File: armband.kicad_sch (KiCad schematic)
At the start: 10 parts, among them IC1 QSMP-1570, SW1 SW_MEC_5G, SW2 SW_MEC_5G

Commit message: progressed charging and gas gauge schematic
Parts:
- added C3, C7: C_Small, symbol Device:C_Small
- renumbered C4 to C1, C3 to C2, R5 to R1, R1 to R2, R2 to R3, R3 to R5, SW2 to SW1, SW1 to SW2
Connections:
- net GND: now also C3.2, C7.2
- net QSMP_VBUS: now also C3.1, C7.1
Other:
- moved on the sheet: C1, R1, R2, R3, SW1

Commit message: added buck
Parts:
- added C5, C8: C_Small, symbol Device:C_Small
- R2, R3: MFN (none) -> 667-ERJ-1GNJ103C
- renumbered C7 to C4
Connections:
- net QSMP_VIN is gone; now on net +3V3: IC1.49 (VIN_1), IC1.50 (VIN_2)
- net +3V3: now also C5.1, C8.1
- net GND: now also C5.2, C8.2
- net QSMP_SCL: now also R2.2; no longer R3.2
- net QSMP_SDA: now also R3.2; no longer R2.2

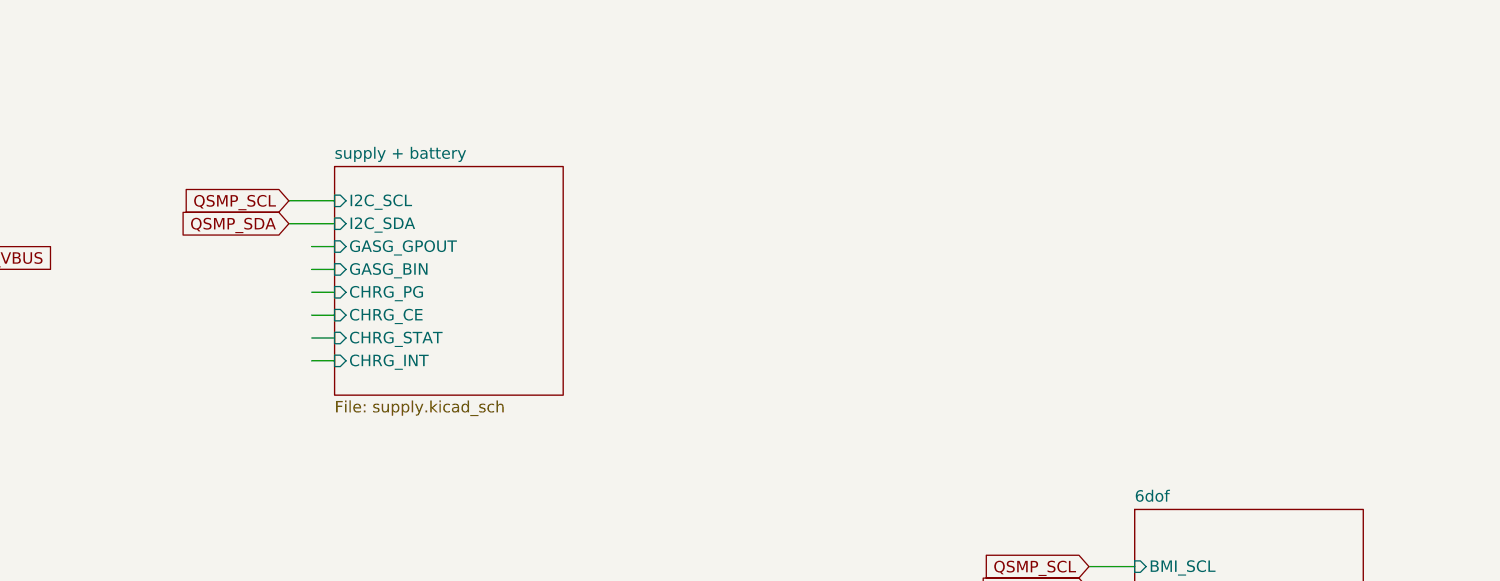
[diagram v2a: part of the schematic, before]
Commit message: added usb connector
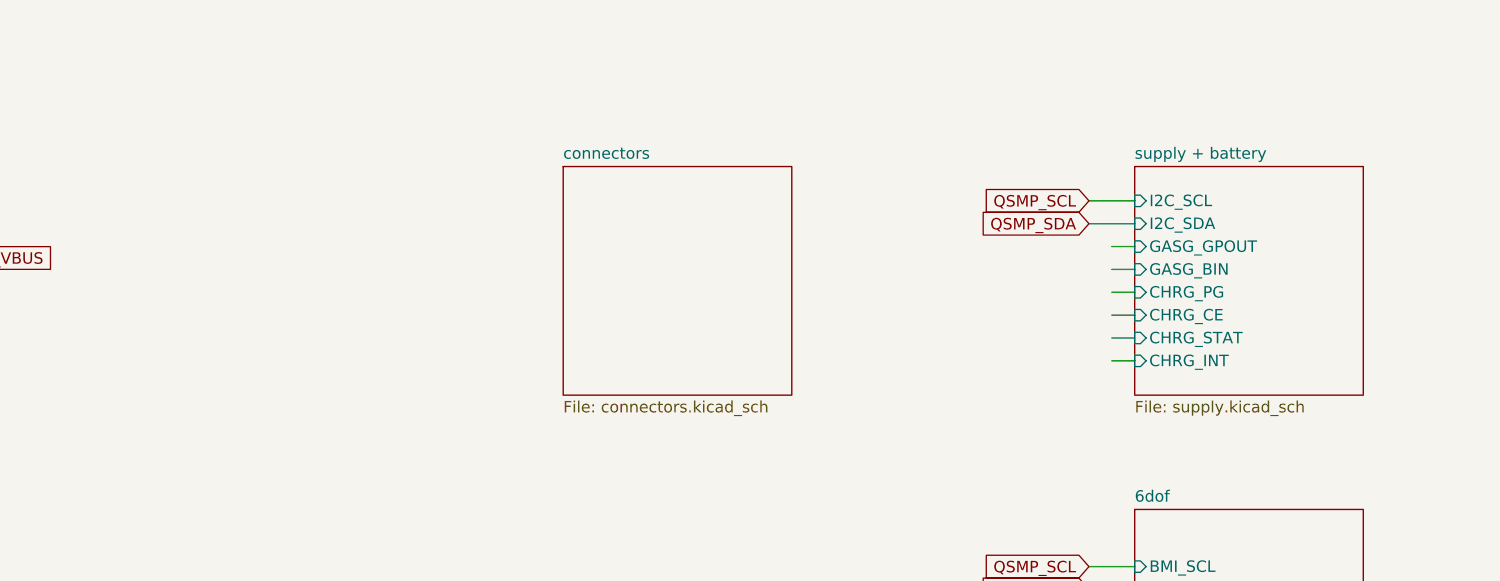
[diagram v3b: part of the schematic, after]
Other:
- added sheet connectors (connectors.kicad_sch)
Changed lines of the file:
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@@
     (stroke (width 0) (type default))
   )
-  (wire (pts (xy 276.86 41.91) (xy 279.4 41.91))
+  (wire (pts (xy 365.76 41.91) (xy 368.3 41.91))
     (stroke (width 0) (type default))
   )
@@
     (stroke (width 0) (type default))
   )
-  (wire (pts (xy 274.32 31.75) (xy 279.4 31.75))
+  (wire (pts (xy 363.22 31.75) (xy 368.3 31.75))
     (stroke (width 0) (type default))
   )
@@
     (stroke (width 0) (type default))
   )
-  (wire (pts (xy 274.32 29.21) (xy 279.4 29.21))
+  (wire (pts (xy 363.22 29.21) (xy 368.3 29.21))
     (stroke (width 0) (type default))
   )
@@
     (stroke (width 0) (type default))
   )
-  (wire (pts (xy 276.86 34.29) (xy 279.4 34.29))
+  (wire (pts (xy 365.76 34.29) (xy 368.3 34.29))
     (stroke (width 0) (type default))
   )
@@
     (stroke (width 0) (type default))
   )
-  (wire (pts (xy 276.86 39.37) (xy 279.4 39.37))
+  (wire (pts (xy 365.76 39.37) (xy 368.3 39.37))
     (stroke (width 0) (type default))
   )
@@
     (stroke (width 0) (type default))
   )
-  (wire (pts (xy 276.86 36.83) (xy 279.4 36.83))
+  (wire (pts (xy 365.76 36.83) (xy 368.3 36.83))
     (stroke (width 0) (type default))
   )
@@
     (stroke (width 0) (type default))
   )
-  (wire (pts (xy 276.86 46.99) (xy 279.4 46.99))
+  (wire (pts (xy 365.76 46.99) (xy 368.3 46.99))
     (stroke (width 0) (type default))
   )
@@
     (stroke (width 0) (type default))
   )
-  (wire (pts (xy 276.86 44.45) (xy 279.4 44.45))
+  (wire (pts (xy 365.76 44.45) (xy 368.3 44.45))
     (stroke (width 0) (type default))
   )
@@
     )
   )
-  (global_label "QSMP_SDA" (shape input) (at 274.32 31.75 180) (fields_autoplaced)
-    (effects (font (size 1.27 1.27)) (justify right))
-    (property "Intersheetrefs" "${INTERSHEET_REFS}" (at 261.6171 31.75 0)
-      (effects (font (size 1.27 1.27)) (justify right) hide)
-    )
-  )
-  (global_label "QSMP_SCL" (shape input) (at 274.32 29.21 180) (fields_autoplaced)
-    (effects (font (size 1.27 1.27)) (justify right))
-    (property "Intersheetrefs" "${INTERSHEET_REFS}" (at 261.6776 29.21 0)
+  (global_label "QSMP_SDA" (shape input) (at 363.22 31.75 180) (fields_autoplaced)
+    (effects (font (size 1.27 1.27)) (justify right))
+    (property "Intersheetrefs" "${INTERSHEET_REFS}" (at 350.5171 31.75 0)
+      (effects (font (size 1.27 1.27)) (justify right) hide)
+    )
+  )
+  (global_label "QSMP_SCL" (shape input) (at 363.22 29.21 180) (fields_autoplaced)
+    (effects (font (size 1.27 1.27)) (justify right))
+    (property "Intersheetrefs" "${INTERSHEET_REFS}" (at 350.5776 29.21 0)
       (effects (font (size 1.27 1.27)) (justify right) hide)
     )
@@
     )
   )
+  (sheet (at 304.8 25.4) (size 25.4 25.4) (fields_autoplaced)
+    (stroke (width 0.1524) (type solid))
+    (fill (color 0 0 0 0.0000))
+    (property "Sheetname" "connectors" (at 304.8 24.6884 0)
+      (effects (font (size 1.27 1.27)) (justify left bottom))
+    )
+    (property "Sheetfile" "connectors.kicad_sch" (at 304.8 51.3846 0)
+      (effects (font (size 1.27 1.27)) (justify left top))
+    )
+    (instances
+      (project "armband"
+        (path "/017c50c6-333c-4d31-ad5a-278994a09b14" (page "8"))
+      )
+    )
+  )
   (sheet (at 368.3 63.5) (size 25.4 25.4) (fields_autoplaced)
     (stroke (width 0.1524) (type solid))
@@
     )
   )
-  (sheet (at 279.4 25.4) (size 25.4 25.4) (fields_autoplaced)
+  (sheet (at 368.3 25.4) (size 25.4 25.4) (fields_autoplaced)
     (stroke (width 0.1524) (type solid))
     (fill (color 0 0 0 0.0000))
-    (property "Sheetname" "supply + battery" (at 279.4 24.6884 0)
+    (property "Sheetname" "supply + battery" (at 368.3 24.6884 0)
       (effects (font (size 1.27 1.27)) (justify left bottom))
     )
-    (property "Sheetfile" "supply.kicad_sch" (at 279.4 51.3846 0)
+    (property "Sheetfile" "supply.kicad_sch" (at 368.3 51.3846 0)
       (effects (font (size 1.27 1.27)) (justify left top))
     )
-    (pin "I2C_SCL" input (at 279.4 29.21 180)
-      (effects (font (size 1.27 1.27)) (justify left))
-    )
-    (pin "I2C_SDA" input (at 279.4 31.75 180)
-      (effects (font (size 1.27 1.27)) (justify left))
-    )
-    (pin "GASG_GPOUT" input (at 279.4 34.29 180)
-      (effects (font (size 1.27 1.27)) (justify left))
-    )
-    (pin "GASG_BIN" input (at 279.4 36.83 180)
-      (effects (font (size 1.27 1.27)) (justify left))
-    )
-    (pin "CHRG_PG" input (at 279.4 39.37 180)
-      (effects (font (size 1.27 1.27)) (justify left))
-    )
-    (pin "CHRG_CE" input (at 279.4 41.91 180)
-      (effects (font (size 1.27 1.27)) (justify left))
-    )
-    (pin "CHRG_STAT" input (at 279.4 44.45 180)
-      (effects (font (size 1.27 1.27)) (justify left))
-    )
-    (pin "CHRG_INT" input (at 279.4 46.99 180)
-      (effects (font (size 1.27 1.27)) (justify left))
-    )
+    (pin "I2C_SCL" input (at 368.3 29.21 180)
+      (effects (font (size 1.27 1.27)) (justify left))
+    )
+    (pin "I2C_SDA" input (at 368.3 31.75 180)
+      (effects (font (size 1.27 1.27)) (justify left))
+    )
+    (pin "GASG_GPOUT" input (at 368.3 34.29 180)
+      (effects (font (size 1.27 1.27)) (justify left))
+    )
+    (pin "GASG_BIN" input (at 368.3 36.83 180)
+      (effects (font (size 1.27 1.27)) (justify left))
+    )
+    (pin "CHRG_PG" input (at 368.3 39.37 180)
+      (effects (font (size 1.27 1.27)) (justify left))
+    )
+    (pin "CHRG_CE" input (at 368.3 41.91 180)
+      (effects (font (size 1.27 1.27)) (justify left))
+    )
+    (pin "CHRG_STAT" input (at 368.3 44.45 180)
+      (effects (font (size 1.27 1.27)) (justify left))
+    )
+    (pin "CHRG_INT" input (at 368.3 46.99 180)
+      (effects (font (size 1.27 1.27)) (justify left))
+    )

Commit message: added usb protection
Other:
- sheet connectors ports: added CC1, CC2, SBU_N, SBU_P, USB_B_N, USB_B_P, USB_FAULT, USB_T_N, USB_T_P, VIN_FAULT; removed none
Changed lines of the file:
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@@
     )
   )
-  (sheet (at 304.8 25.4) (size 25.4 25.4) (fields_autoplaced)
+  (sheet (at 317.5 25.4) (size 25.4 25.4) (fields_autoplaced)
     (stroke (width 0.1524) (type solid))
     (fill (color 0 0 0 0.0000))
-    (property "Sheetname" "connectors" (at 304.8 24.6884 0)
+    (property "Sheetname" "connectors" (at 317.5 24.6884 0)
       (effects (font (size 1.27 1.27)) (justify left bottom))
     )
-    (property "Sheetfile" "connectors.kicad_sch" (at 304.8 51.3846 0)
+    (property "Sheetfile" "connectors.kicad_sch" (at 317.5 51.3846 0)
       (effects (font (size 1.27 1.27)) (justify left top))
     )
+    (pin "VIN_FAULT" input (at 317.5 46.99 180)
+      (effects (font (size 1.27 1.27)) (justify left))
+    )
+    (pin "USB_T_N" input (at 317.5 29.21 180)
+      (effects (font (size 1.27 1.27)) (justify left))
+    )
+    (pin "USB_T_P" input (at 317.5 26.67 180)
+      (effects (font (size 1.27 1.27)) (justify left))
+    )
+    (pin "USB_B_P" input (at 317.5 31.75 180)
+      (effects (font (size 1.27 1.27)) (justify left))
+    )
+    (pin "USB_B_N" input (at 317.5 34.29 180)
+      (effects (font (size 1.27 1.27)) (justify left))
+    )
+    (pin "CC2" input (at 317.5 39.37 180)
+      (effects (font (size 1.27 1.27)) (justify left))
+    )
+    (pin "SBU_N" input (at 317.5 44.45 180)
+      (effects (font (size 1.27 1.27)) (justify left))
+    )
+    (pin "SBU_P" input (at 317.5 41.91 180)
+      (effects (font (size 1.27 1.27)) (justify left))
+    )
+    (pin "CC1" input (at 317.5 36.83 180)
+      (effects (font (size 1.27 1.27)) (justify left))
+    )
+    (pin "USB_FAULT" input (at 317.5 49.53 180)
+      (effects (font (size 1.27 1.27)) (justify left))
+    )
     (instances

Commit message: finished usb connection ciruits
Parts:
- removed C3, C4: C_Small, symbol Device:C_Small
- added C25: 100n 16V, Capacitor_SMD:C_0402_1005Metric, symbol Device:C_Small
- added C27: 1u 6.3V, Capacitor_SMD:C_0201_0603Metric, symbol Device:C_Small
- C5: value C_Small -> 1u 6.3V; footprint (none) -> Capacitor_SMD:C_0201_0603Metric; MFN (none) -> 710-885012104011
- C8: value C_Small -> 100n 16V; footprint (none) -> Capacitor_SMD:C_0402_1005Metric; MFN (none) -> 80-C0402C104M4V
- R5: footprint Resistor_SMD:R_0402_1005Metric -> Resistor_SMD:R_0201_0603Metric; MFN (none) -> 603-AC0201JR-070RL
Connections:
- net +3V3: now also C25.1, C27.1; no longer C5.1, C8.1
- net GND: now also C25.2, C27.2
- net QSMP_VBUS: now also C5.1, C8.1
- net QSMP_USB_DN: now reaches IC1.47 (USBB_DN)
- net QSMP_USB_DP: now reaches IC1.48 (USBB_DP)
- net QSMP_RXD: now reaches IC1.89 (UARTA_RXD)
- net QSMP_TXD: now reaches IC1.90 (UARTA_TXD)
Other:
- sheet connectors renamed usb
- sheet debug ports: added RXD, TXD; removed none
- sheet usb: file connectors.kicad_sch -> usb.kicad_sch
- sheet usb ports: added none; removed CC1, CC2, SBU_N, SBU_P
- note added: "Supply"
- moved on the sheet: C1, C2, R1, R2, R3, R4, SW1, SW2
